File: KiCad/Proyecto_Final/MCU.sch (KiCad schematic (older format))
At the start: 42 parts

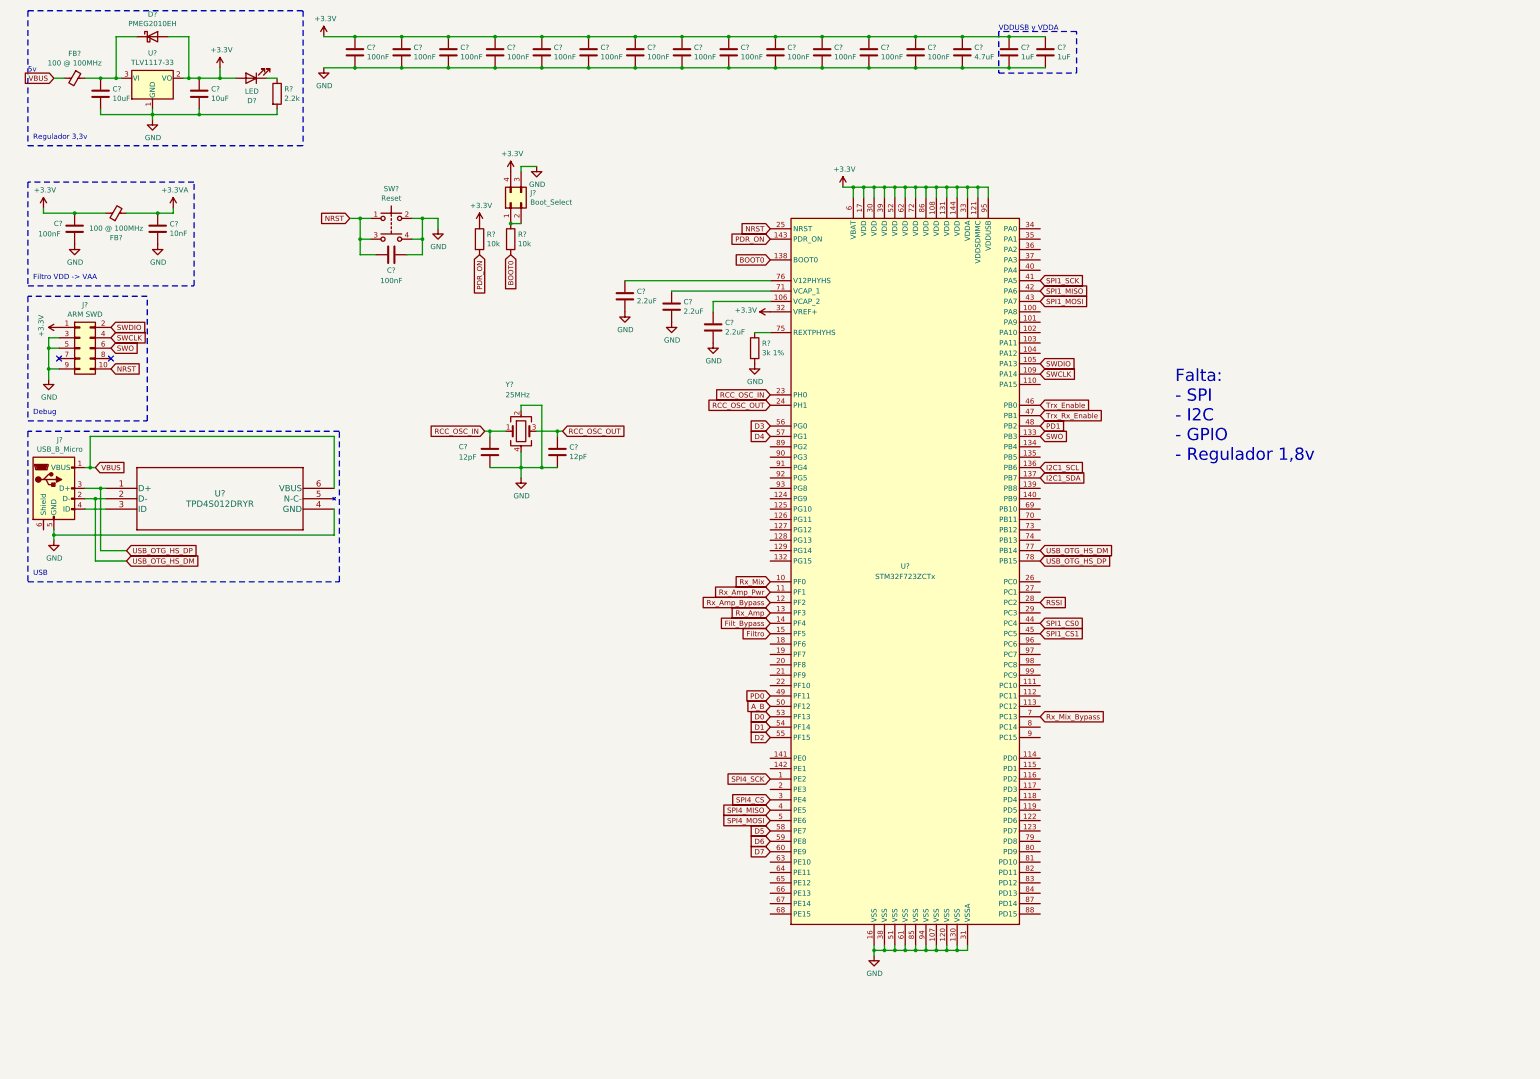
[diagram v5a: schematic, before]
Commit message: Update esquemático, reubicación de archivos Gantt.
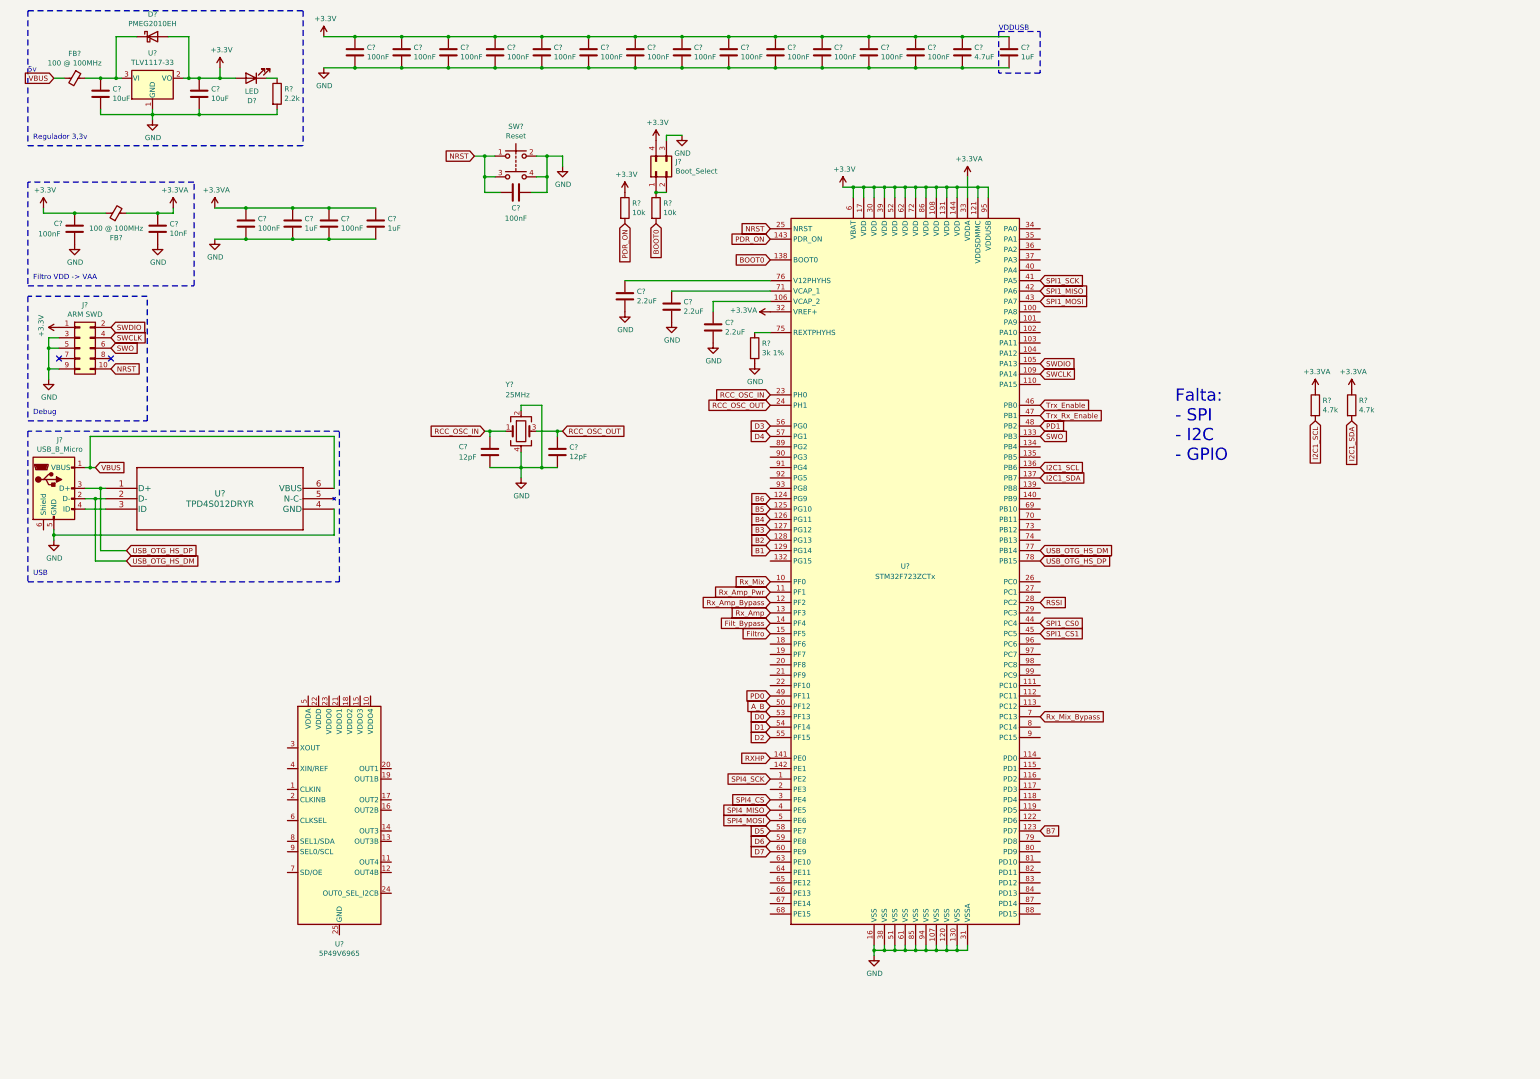
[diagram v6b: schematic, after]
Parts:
- removed C?: 1uF, symbol Device:C
- added C? (x2): 100nF, symbol Device:C
- added C? (x2): 1uF, symbol Device:C
- added R? (x2): 4.7k, symbol Device:R
- added U?: 5P49V6965, Package_DFN_QFN:QFN-24-1EP_4x4mm_P0.5mm_EP2.8x2.8mm, symbol Oscillator:5P49V6965
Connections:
- net +3.3VA: now also U?.32 (VREF+), U?.33 (VDDA), C?.1, C?.1, C?.1, C?.1, R?.1, R?.1
- net +3V3: no longer U?.32 (VREF+), U?.33 (VDDA)
- net GND: now also C?.2, C?.2, C?.2, C?.2
- net I2C1_SCL: now also R?.2
- net I2C1_SDA: now also R?.2
- net B7: now reaches U?.123 (PD7)
- net B6: now reaches U?.124 (PG9)
- net B5: now reaches U?.125 (PG10)
- net B4: now reaches U?.126 (PG11)
- net B3: now reaches U?.127 (PG12)
- net B2: now reaches U?.128 (PG13)
- net B1: now reaches U?.129 (PG14)
- net RXHP: now reaches U?.141 (PE0)
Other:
- note added: "Falta:\n- SPI\n- I2C\n- GPIO"
- note added: "VDDUSB"
- note removed: "Falta:\n- SPI\n- I2C\n- GPIO\n- Regulador 1,8v"
- note removed: "VDDUSB y VDDA"
- moved on the sheet: C?, J?, R?, SW?

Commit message: Agregado generador de clock.
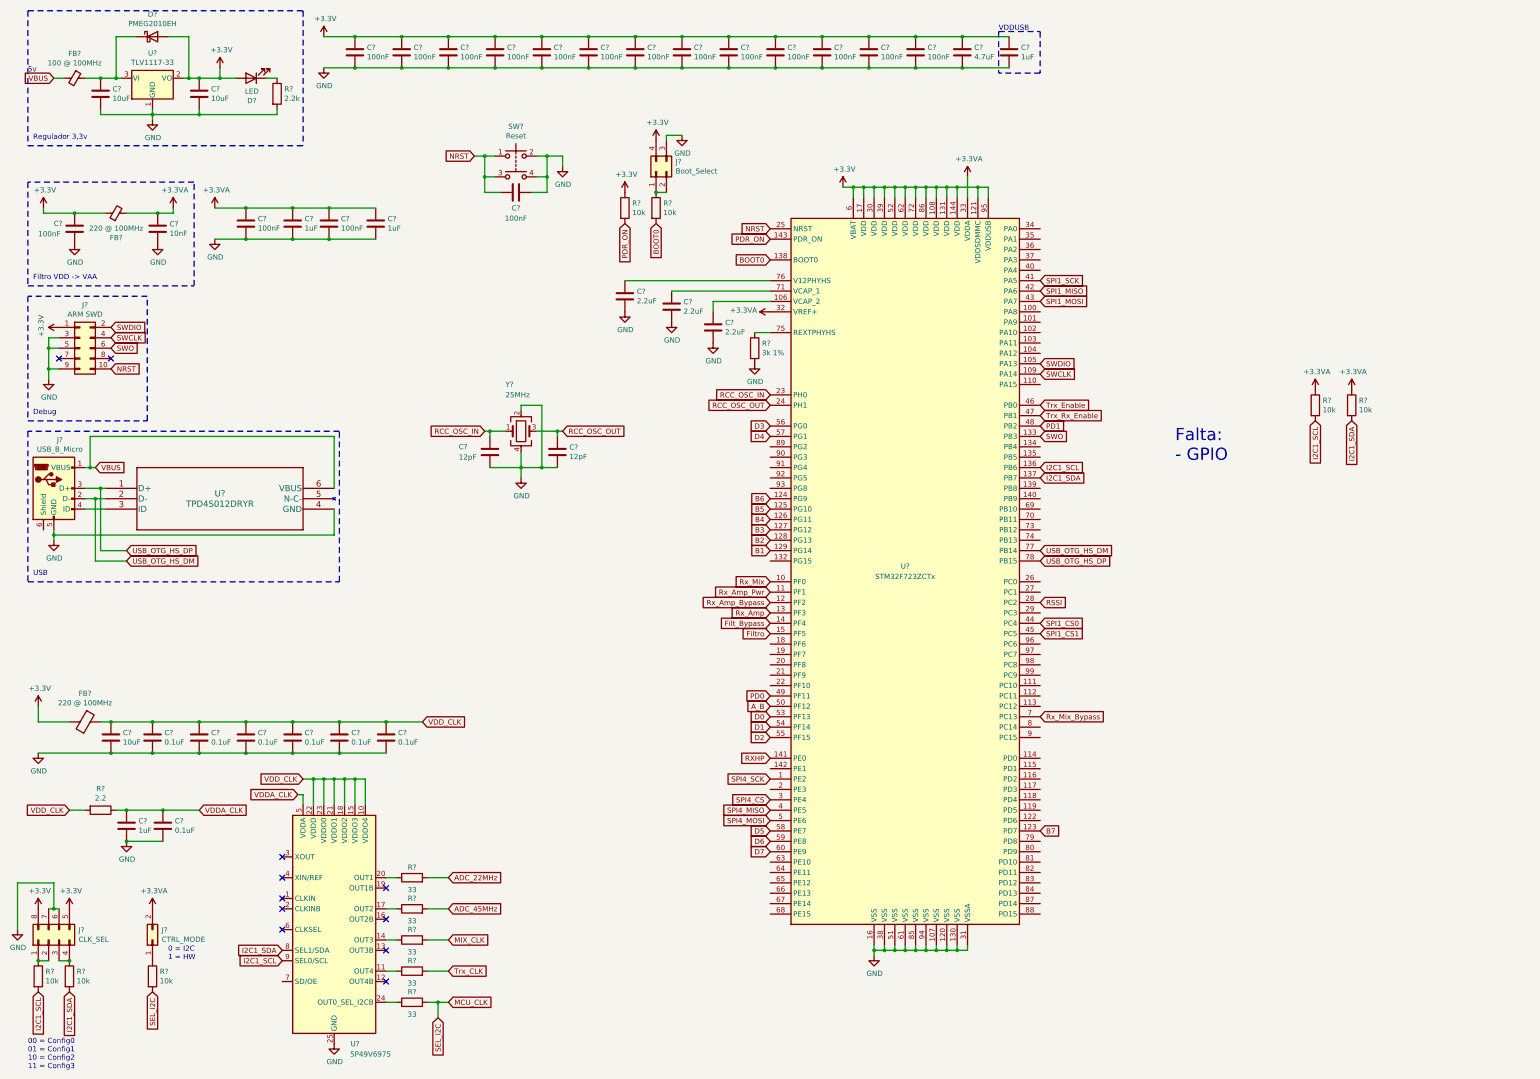
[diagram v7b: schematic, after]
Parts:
- added C?: 10uF, symbol Device:C
- added C? (x7): 0.1uF, symbol Device:C
- added C?: 1uF, symbol Device:C
- added FB?: 220 @ 100MHz, symbol Device:Ferrite_Bead
- added J?: CLK_SEL, symbol Connector_Generic:Conn_02x04_Counter_Clockwise
- added J?: CTRL_MODE, symbol Connector_Generic:Conn_02x01
- added R?: 2.2, symbol Device:R
- added R? (x5): 33, symbol Device:R
- added R? (x3): 10k, symbol Device:R
- FB?: value 100 @ 100MHz -> 220 @ 100MHz
- R? (x2): value 4.7k -> 10k
- U?: value 5P49V6965 -> 5P49V6975
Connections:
- net +3.3VA: now also J?.2 (Pin_2)
- net +3V3: now also FB?.2, J?.5 (Pin_5), J?.8 (Pin_8)
- net GND: now also U?.25 (GND), C?.2, C?.2, C?.2, C?.2, C?.2, C?.2, C?.2, C?.2, C?.2, J?.6 (Pin_6), J?.7 (Pin_7)
- net I2C1_SCL: now also U?.9 (SEL0/SCL), R?.2
- net I2C1_SDA: now also U?.8 (SEL1/SDA), R?.2
- net VDD_CLK: now reaches U?.10 (VDDO4)
- net VDD_CLK: now also U?.15 (VDDO3), U?.18 (VDDO2), U?.21 (VDDO1), U?.22 (VDDD), U?.23 (VDDO0), C?.1, C?.1, C?.1, C?.1, C?.1, C?.1, C?.1, FB?.1, R?.2
- net at U?.11 (OUT4): now also R?.1
- net at U?.14 (OUT3): now also R?.1
- net at U?.17 (OUT2): now also R?.1
- net at U?.20 (OUT1): now also R?.1
- net at U?.24 (OUT0_SEL_I2CB): now also R?.1
- net VDDA_CLK: now reaches U?.5 (VDDA)
- net VDDA_CLK: now also C?.1, C?.1, R?.1
- new net: J?.1 (Pin_1), R?.1
- new net: J?.1 (Pin_1), J?.2 (Pin_2), R?.1
- new net: J?.3 (Pin_3), J?.4 (Pin_4), R?.1
- new net ADC_22MHz: R?.2
- new net ADC_45MHz: R?.2
- new net MCU_CLK: R?.2, R?.2
- new net MIX_CLK: R?.2
- new net Trx_CLK: R?.2
- no-connect marks 2 -> 11
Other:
- note added: "0 = I2C\n1 = HW"
- note added: "00 = Config0\n01 = Config1\n10 = Config2\n11 = Config3"
- note added: "Falta:\n- GPIO"
- note removed: "Falta:\n- SPI\n- I2C\n- GPIO"
- moved on the sheet: U?

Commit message: Terminado esquematico.
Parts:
- removed C? (x2): 12pF, symbol Device:C
- removed FB?: 100 @ 100MHz, symbol Device:Ferrite_Bead_Small
- removed Y?: 25MHz, symbol Device:Crystal_GND24
- added FB?: 220 @ 100MHz, symbol Device:Ferrite_Bead
- added J?: PG, symbol Connector_Generic:Conn_02x03_Top_Bottom
- added J?: PF, symbol Connector_Generic:Conn_02x03_Top_Bottom
- added J?: PE, symbol Connector_Generic:Conn_02x04_Top_Bottom
- added J?: PD, symbol Connector_Generic:Conn_02x08_Top_Bottom
- added J?: PC, symbol Connector_Generic:Conn_02x06_Top_Bottom
- added J?: PB, symbol Connector_Generic:Conn_02x04_Top_Bottom
- added J?: PA, symbol Connector_Generic:Conn_02x06_Top_Bottom
- added J?: SPI4, symbol Connector_Generic:Conn_01x04
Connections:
- net RCC_OSC_IN is gone; now on net MCU_CLK: U?.23 (PH0)
- net PD0: now also U?.114 (PD0), J?.1 (Pin_1)
- net PD1: now also U?.115 (PD1), J?.2 (Pin_2)
- net SPI4_CS: now also J?.4 (Pin_4)
- net SPI4_MISO: now also J?.3 (Pin_3)
- net SPI4_MOSI: now also J?.2 (Pin_2)
- net SPI4_SCK: now also J?.1 (Pin_1)
- net VBUS: now also FB?.2
- net PA8: now reaches U?.100 (PA8)
- net PA8: now also J?.6 (Pin_6)
- net PA9: now reaches U?.101 (PA9)
- net PA9: now also J?.7 (Pin_7)
- net PA10: now reaches U?.102 (PA10)
- net PA10: now also J?.8 (Pin_8)
- net PA11: now reaches U?.103 (PA11)
- net PA11: now also J?.9 (Pin_9)
- net PA12: now reaches U?.104 (PA12)
- net PA12: now also J?.10 (Pin_10)
- net PA15: now reaches U?.110 (PA15)
- net PA15: now also J?.11 (Pin_11)
- net PC10: now reaches U?.111 (PC10)
- net PC10: now also J?.8 (Pin_8)
- net PC11: now reaches U?.112 (PC11)
- net PC11: now also J?.9 (Pin_9)
- net PC12: now reaches U?.113 (PC12)
- net PC12: now also J?.10 (Pin_10)
- net PD2: now reaches U?.116 (PD2)
- net PD2: now also J?.3 (Pin_3)
- net PD3: now reaches U?.117 (PD3)
- net PD3: now also J?.4 (Pin_4)
- net PD4: now reaches U?.118 (PD4)
- net PD4: now also J?.5 (Pin_5)
- net PD5: now reaches U?.119 (PD5)
- net PD5: now also J?.6 (Pin_6)
- net PD6: now reaches U?.122 (PD6)
- net PD6: now also J?.7 (Pin_7)
- net PG15: now reaches U?.132 (PG15)
- net PG15: now also J?.6 (Pin_6)
- net PB4: now reaches U?.134 (PB4)
- net PB4: now also J?.1 (Pin_1)
- net PB5: now reaches U?.135 (PB5)
- net PB5: now also J?.2 (Pin_2)
- net PB8: now reaches U?.139 (PB8)
- net PB8: now also J?.3 (Pin_3)
- net PB9: now reaches U?.140 (PB9)
- net PB9: now also J?.4 (Pin_4)
- net PE1: now reaches U?.142 (PE1)
- net PE1: now also J?.1 (Pin_1)
- net PF6: now reaches U?.18 (PF6)
- net PF6: now also J?.1 (Pin_1)
- net PF7: now reaches U?.19 (PF7)
- net PF7: now also J?.2 (Pin_2)
- net PE3: now reaches U?.2 (PE3)
- net PE3: now also J?.2 (Pin_2)
- net PF8: now reaches U?.20 (PF8)
- net PF8: now also J?.3 (Pin_3)
- net PF9: now reaches U?.21 (PF9)
- net PF9: now also J?.4 (Pin_4)
- net PF10: now reaches U?.22 (PF10)
- net PF10: now also J?.5 (Pin_5)
- net PC0: now reaches U?.26 (PC0)
- net PC0: now also J?.1 (Pin_1)
- net PC1: now reaches U?.27 (PC1)
- net PC1: now also J?.2 (Pin_2)
- net PC3: now reaches U?.29 (PC3)
- net PC3: now also J?.3 (Pin_3)
- net PA0: now reaches U?.34 (PA0)
- net PA0: now also J?.1 (Pin_1)
- net PA1: now reaches U?.35 (PA1)
- net PA1: now also J?.2 (Pin_2)
- net PA2: now reaches U?.36 (PA2)
- net PA2: now also J?.3 (Pin_3)
- net PA3: now reaches U?.37 (PA3)
- net PA3: now also J?.4 (Pin_4)
- net PA4: now reaches U?.40 (PA4)
- net PA4: now also J?.5 (Pin_5)
- net PE10: now reaches U?.63 (PE10)
- net PE10: now also J?.3 (Pin_3)
- net PE11: now reaches U?.64 (PE11)
- net PE11: now also J?.4 (Pin_4)
- net PE12: now reaches U?.65 (PE12)
- net PE12: now also J?.5 (Pin_5)
- net PE13: now reaches U?.66 (PE13)
- net PE13: now also J?.6 (Pin_6)
- net PE14: now reaches U?.67 (PE14)
- net PE14: now also J?.7 (Pin_7)
- net PE15: now reaches U?.68 (PE15)
- net PE15: now also J?.8 (Pin_8)
- net PB10: now reaches U?.69 (PB10)
- net PB10: now also J?.5 (Pin_5)
- net PB11: now reaches U?.70 (PB11)
- net PB11: now also J?.6 (Pin_6)
- net PB12: now reaches U?.73 (PB12)
- net PB12: now also J?.7 (Pin_7)
- net PB13: now reaches U?.74 (PB13)
- net PB13: now also J?.8 (Pin_8)
- net PD8: now reaches U?.79 (PD8)
- net PD8: now also J?.8 (Pin_8)
- net PC14: now reaches U?.8 (PC14)
- net PC14: now also J?.11 (Pin_11)
- net PD9: now reaches U?.80 (PD9)
- net PD9: now also J?.9 (Pin_9)
- net PD10: now reaches U?.81 (PD10)
- net PD10: now also J?.10 (Pin_10)
- net PD11: now reaches U?.82 (PD11)
- net PD11: now also J?.11 (Pin_11)
- net PD12: now reaches U?.83 (PD12)
- net PD12: now also J?.12 (Pin_12)
- net PD13: now reaches U?.84 (PD13)
- net PD13: now also J?.13 (Pin_13)
- net PD14: now reaches U?.87 (PD14)
- net PD14: now also J?.14 (Pin_14)
- net PD15: now reaches U?.88 (PD15)
- net PD15: now also J?.15 (Pin_15)
- net PG2: now reaches U?.89 (PG2)
- net PG2: now also J?.1 (Pin_1)
- net PC15: now reaches U?.9 (PC15)
- net PC15: now also J?.12 (Pin_12)
- net PG3: now reaches U?.90 (PG3)
- net PG3: now also J?.2 (Pin_2)
- net PG4: now reaches U?.91 (PG4)
- net PG4: now also J?.3 (Pin_3)
- net PG5: now reaches U?.92 (PG5)
- net PG5: now also J?.4 (Pin_4)
- net PG8: now reaches U?.93 (PG8)
- net PG8: now also J?.5 (Pin_5)
- net PC6: now reaches U?.96 (PC6)
- net PC6: now also J?.4 (Pin_4)
- net PC7: now reaches U?.97 (PC7)
- net PC7: now also J?.5 (Pin_5)
- net PC8: now reaches U?.98 (PC8)
- net PC8: now also J?.6 (Pin_6)
- net PC9: now reaches U?.99 (PC9)
- net PC9: now also J?.7 (Pin_7)
- net at C?.1, D?.1 (K), U?.3 (VI): now also FB?.1
- net RCC_OSC_OUT: no longer names the net of U?.24 (PH1)
- no-connect marks 11 -> 15
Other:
- note removed: "Falta:\n- GPIO"
- moved on the sheet: C?, D?, J?, R?, SW?, U?
